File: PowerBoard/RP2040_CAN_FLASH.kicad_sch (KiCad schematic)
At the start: 48 parts, among them J1 B3B-XH-A_LF__SN_, J2 USB4145-03-0170-C_REVA2, J4 B3B-XH-A_LF__SN_, J5 Conn_02x10_Counter_Clockwise, Q1 BSS138, Q4 BSS138, U1 RPI2040, U5 W25Q128JVS, U7 MCP2515-xST, U8 MCP2551-I-SN, Y1 445C25D12M00000, Y2 CX532Z-A2B3C5-70-8.0D18

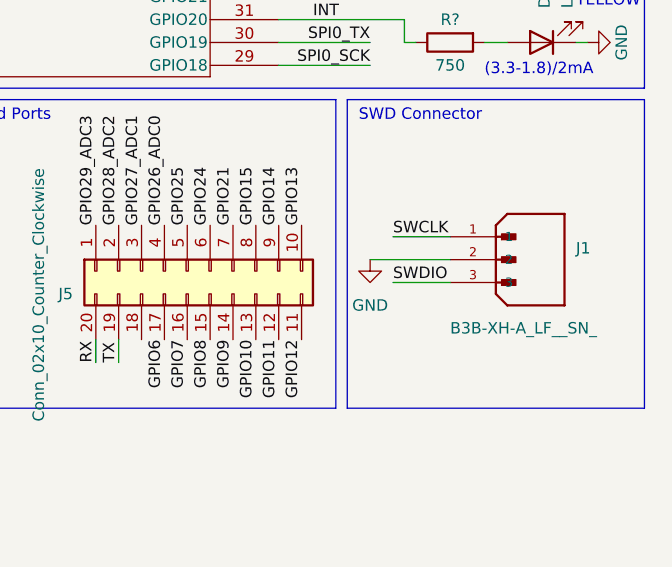
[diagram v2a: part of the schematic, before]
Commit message: layout v1 complete
- consider adding a auto discharge circuit
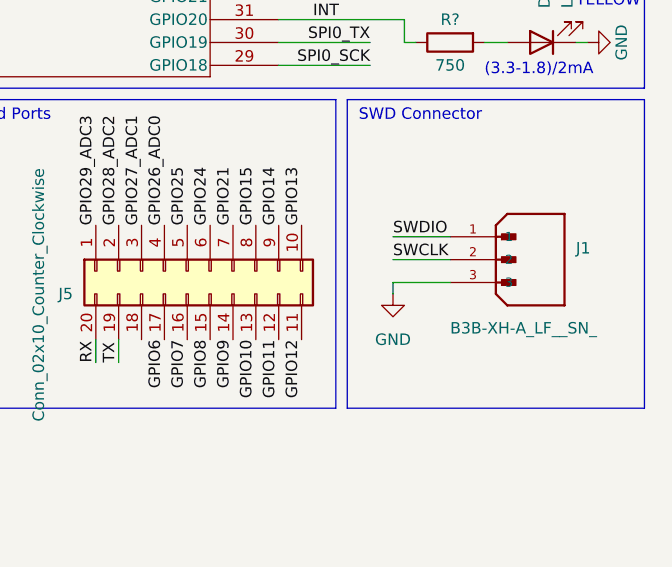
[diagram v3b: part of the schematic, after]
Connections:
- net GND: now also J1.3; no longer J1.2
- net SWCLK: now also J1.2; no longer J1.1
- net SWDIO: now also J1.1; no longer J1.3
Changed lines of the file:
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@@
+    (stroke (width 0) (type default))
+  )
+  (wire (pts (xy 251.46 149.86) (xy 257.81 149.86))
     (stroke (width 0) (type default))
   )
@@
     (stroke (width 0) (type default))
   )
-  (wire (pts (xy 248.92 147.32) (xy 257.81 147.32))
-    (stroke (width 0) (type default))
-  )
   (wire (pts (xy 88.9 175.26) (xy 82.55 175.26))
     (stroke (width 0) (type default))
@@
     (stroke (width 0) (type default))
   )
-  (wire (pts (xy 251.46 149.86) (xy 257.81 149.86))
+  (wire (pts (xy 251.46 147.32) (xy 257.81 147.32))
     (stroke (width 0) (type default))
   )
@@
   )
   (wire (pts (xy 238.76 74.93) (xy 247.65 74.93))
+    (stroke (width 0) (type default))
+  )
+  (wire (pts (xy 251.46 149.86) (xy 251.46 151.13))
     (stroke (width 0) (type default))
   )
@@
     (effects (font (size 1.27 1.27)) (justify left bottom))
   )
+  (label "SWDIO" (at 251.46 144.78 0) (fields_autoplaced)
+    (effects (font (size 1.27 1.27)) (justify left bottom))
+  )
   (label "QSPI_SCLK" (at 49.53 102.87 0) (fields_autoplaced)
     (effects (font (size 1.27 1.27)) (justify left bottom))
@@
     (effects (font (size 1.27 1.27)) (justify right bottom))
   )
-  (label "SWCLK" (at 251.46 144.78 0) (fields_autoplaced)
-    (effects (font (size 1.27 1.27)) (justify left bottom))
-  )
   (label "GPIO29_ADC3" (at 242.57 95.25 0) (fields_autoplaced)
     (effects (font (size 1.27 1.27)) (justify left bottom))
@@
     (effects (font (size 1.27 1.27)) (justify right bottom))
   )
+  (label "SWCLK" (at 251.46 147.32 0) (fields_autoplaced)
+    (effects (font (size 1.27 1.27)) (justify left bottom))
+  )
   (label "GPIO26_ADC0" (at 226.06 143.51 90) (fields_autoplaced)
-    (effects (font (size 1.27 1.27)) (justify left bottom))
-  )
-  (label "SWDIO" (at 251.46 149.86 0) (fields_autoplaced)
     (effects (font (size 1.27 1.27)) (justify left bottom))
   )
@@
     )
   )
-  (symbol (lib_id "power:GND") (at 248.92 147.32 0) (unit 1)
+  (symbol (lib_id "power:GND") (at 251.46 151.13 0) (unit 1)
     (in_bom yes) (on_board yes) (dnp no) (fields_autoplaced)
-    (property "Reference" "#PWR?" (at 248.92 153.67 0)
-      (effects (font (size 1.27 1.27)) hide)
-    )
-    (property "Value" "GND" (at 248.92 152.4 0)
-      (effects (font (size 1.27 1.27)))
-    )
-    (property "Footprint" "" (at 248.92 147.32 0)
-      (effects (font (size 1.27 1.27)) hide)
-    )
-    (property "Datasheet" "" (at 248.92 147.32 0)
-      (effects (font (size 1.27 1.27)) hide)
-    )
+    (property "Reference" "#PWR?" (at 251.46 157.48 0)
+      (effects (font (size 1.27 1.27)) hide)
+    )
+    (property "Value" "GND" (at 251.46 156.21 0)
+      (effects (font (size 1.27 1.27)))
+    )
+    (property "Footprint" "" (at 251.46 151.13 0)
+      (effects (font (size 1.27 1.27)) hide)
+    )
+    (property "Datasheet" "" (at 251.46 151.13 0)
+      (effects (font (size 1.27 1.27)) hide)
+    )

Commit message: auto discharge circuit
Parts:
- removed J4: B3B-XH-A_LF__SN_, bots:JST_B3B-XH-A_LF__SN_, symbol bots:B3B-XH-A_LF__SN_
- added TP1: SCK, bots:TestPoint_Pad_1.0x1.0mm, symbol Connector:TestPoint
- added TP1: CS, bots:TestPoint_Pad_1.0x1.0mm, symbol Connector:TestPoint
- added TP1: SO, bots:TestPoint_Pad_1.0x1.0mm, symbol Connector:TestPoint
- added TP1: RESET, bots:TestPoint_Pad_1.0x1.0mm, symbol Connector:TestPoint
- added TP1: CANL, bots:TestPoint_THTPad_D1.0mm_Drill0.5mm, symbol Connector:TestPoint
- added TP1: RXCAN, bots:TestPoint_Pad_1.0x1.0mm, symbol Connector:TestPoint
- added TP1: TXCAN, bots:TestPoint_Pad_1.0x1.0mm, symbol Connector:TestPoint
- added TP1: BOOT, bots:TestPoint_Pad_1.0x1.0mm, symbol Connector:TestPoint
- added TP1: 5V, bots:TestPoint_Pad_1.0x1.0mm, symbol Connector:TestPoint
- added TP1: SI, bots:TestPoint_Pad_1.0x1.0mm, symbol Connector:TestPoint
- added TP1: CANH, bots:TestPoint_THTPad_D1.0mm_Drill0.5mm, symbol Connector:TestPoint
- added U10, U9: PTS647SM38SMTR2LFS, SW_PTS647SM38SMTR2LFS_CNK, symbol bots:PTS647SM38SMTR2LFS
- D5: footprint bots:D_SMB -> Diode_SMD:D_SMB
- J1: footprint bots:JST_B3B-XH-A_LF__SN_ -> B3B-XH-A_LF__SN_:JST_B3B-XH-A_LF__SN_
- Q1, Q4: footprint bots:SOT95P240X111-3N -> BSS138:SOT95P240X111-3N
- U7: footprint bots:TSSOP-20_4.4x6.5mm_P0.65mm -> Package_SO:TSSOP-20_4.4x6.5mm_P0.65mm
- U8: footprint bots:SOIC-8_3.9x4.9mm_P1.27mm -> Package_SO:SOIC-8_3.9x4.9mm_P1.27mm
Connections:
- net 5V_USB: now also TP1.1
- net CANH: now also TP1.1
- net CANL: now also TP1.1
- net GND: now also U10.3, U10.4, U9.3, U9.4
- net RUN: now also TP1.1, U9.1, U9.2
- net RXCAN: now also TP1.1
- net SPI0_CS: now also TP1.1
- net SPI0_RX: now also TP1.1
- net SPI0_SCK: now also TP1.1
- net SPI0_TX: now also TP1.1
- net TXCAN: now also TP1.1
- net USB_BOOT renamed BOOT
- net BOOT: now also TP1.1, U10.1, U10.2
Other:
- note added: "BOOT BUTTON"
- note added: "RESET BUTTON"
- moved on the sheet: C?, R?, Y2

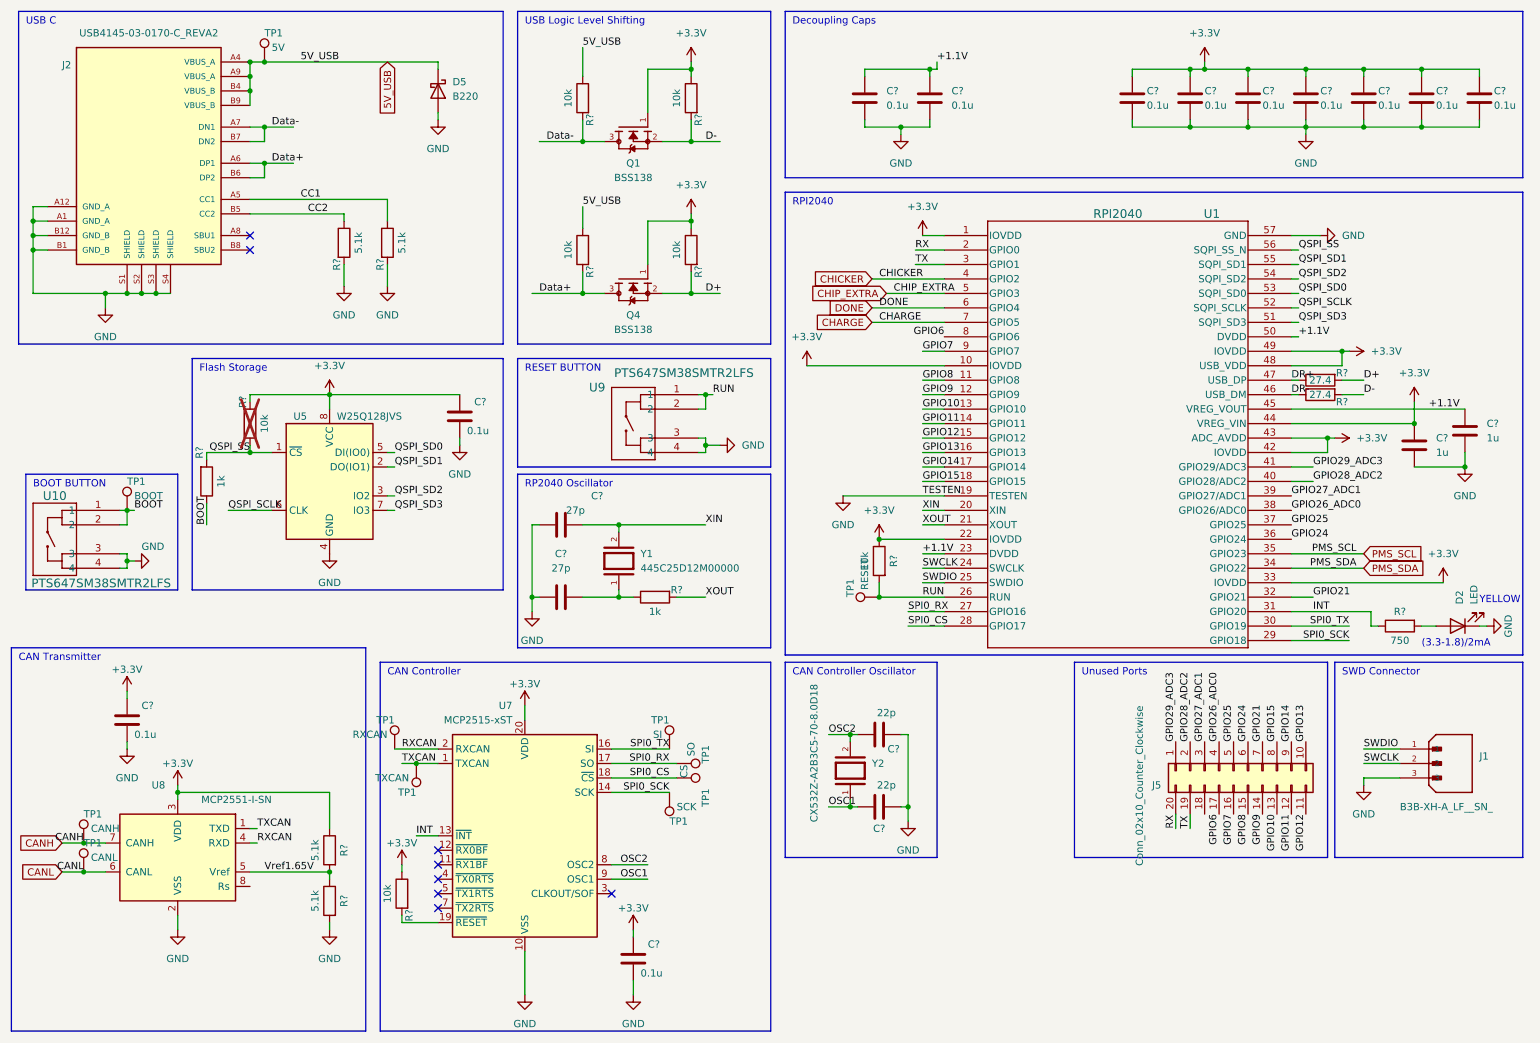
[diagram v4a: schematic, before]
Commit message: updated board edge clearance and cap model
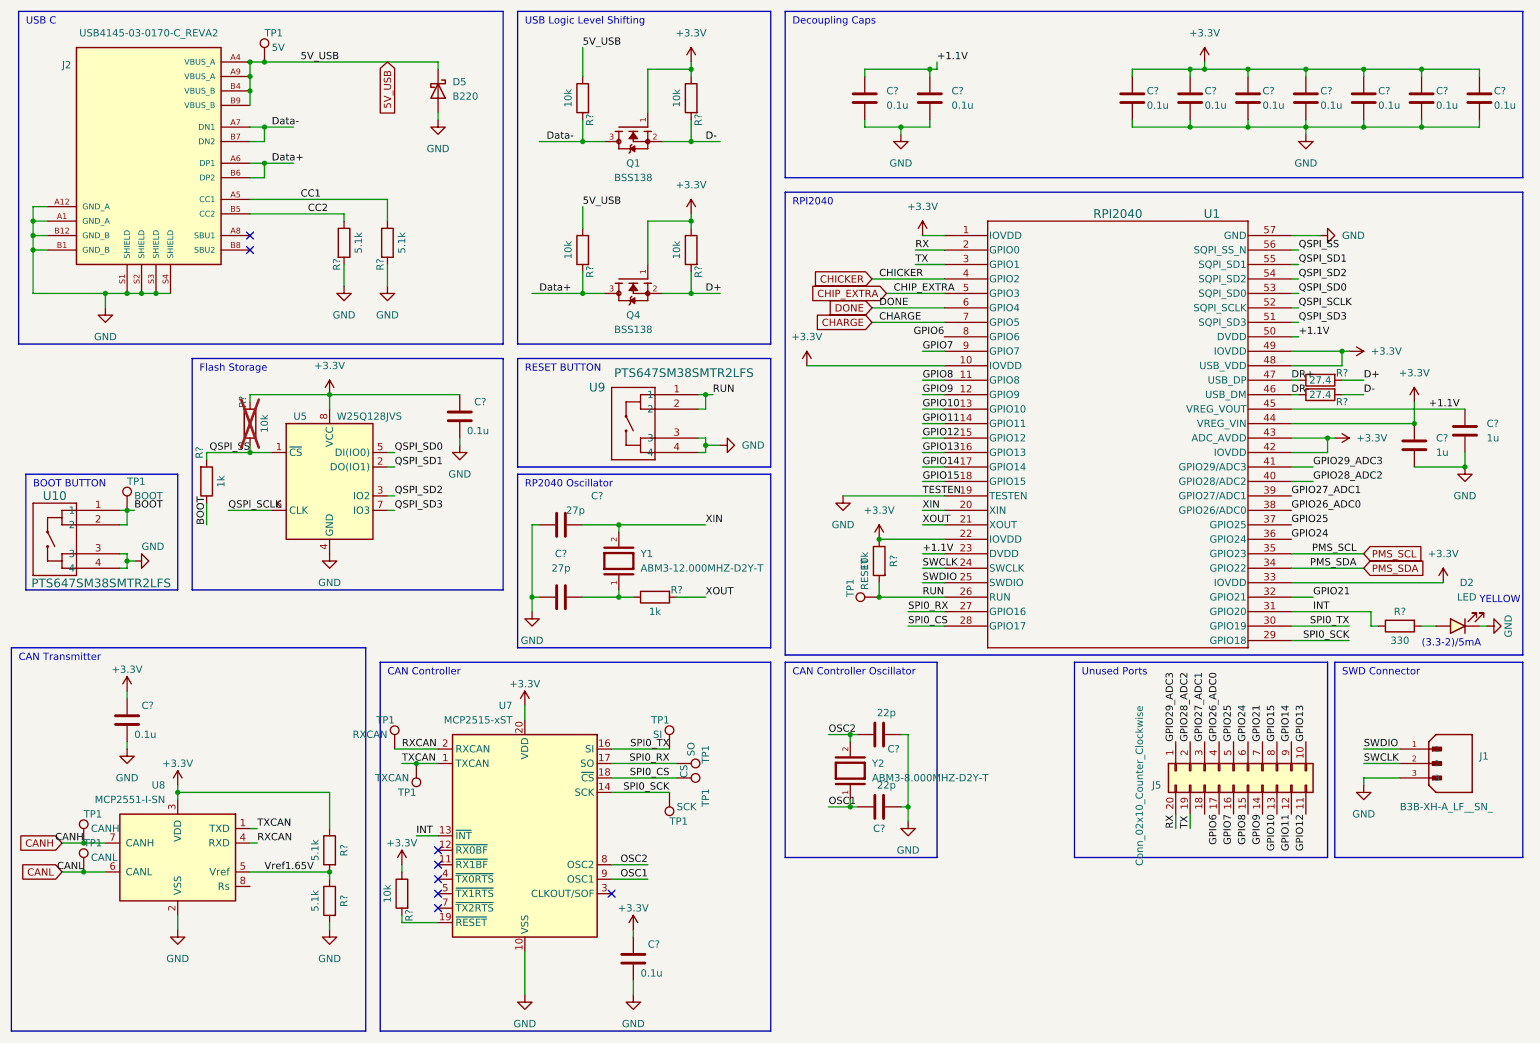
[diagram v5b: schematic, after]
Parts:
- removed D5: B220, Diode_SMD:D_SMB, symbol Diode:B220
- removed U8: MCP2551-I-SN, Package_SO:SOIC-8_3.9x4.9mm_P1.27mm, symbol Interface_CAN_LIN:MCP2551-I-SN
- removed Y1: 445C25D12M00000, bots:445C25D12M00000, symbol bots:445C25D12M00000
- removed Y2: CX532Z-A2B3C5-70-8.0D18, bots:445C25D12M00000, symbol bots:CX532Z-A2B3C5-70-8.0D18
- added D5: B220, bots:D_SMB, symbol bots:B220
- added U8: MCP2551-I-SN, bots:SOIC-8_3.9x4.9mm_P1.27mm, symbol bots:MCP2551-I-SN
- added Y1: ABM3-12.000MHZ-D2Y-T, bots:ABM3, symbol bots:ABM3-12.000MHZ-D2Y-T
- added Y2: ABM3-8.000MHZ-D2Y-T, bots:445C25D12M00000, symbol bots:ABM3-8.000MHZ-D2Y-T
- C? (x2): symbol Device:C -> bots:C_22p; JLC (none) -> 0603; LCSC (none) -> C1653; MPN (none) -> CL10C220JB8NNNC; Manufacturer (none) -> Samsung Electro-Mechanics; Price (none) -> 0.0052
- C? (x12): symbol Device:C -> bots:C_0.1u; JLC (none) -> 0603; LCSC (none) -> C14663; MPN (none) -> CC0603KRX7R9BB104; Manufacturer (none) -> YAGEO; Price (none) -> 0.0021
- C? (x2): symbol Device:C -> bots:C_1u; JLC (none) -> 0603; LCSC (none) -> C15849; MPN (none) -> CL10A105KB8NNNC; Manufacturer (none) -> Samsung Electro-Mechanics; Price (none) -> 0.0046
- C? (x2): symbol Device:C -> bots:C_27p; JLC (none) -> 0603; LCSC (none) -> C107045; MPN (none) -> CC0603JRNPO9BN270; Manufacturer (none) -> YAGEO; Price (none) -> 0.0027
- D2: footprint bots:LED_1206_3216Metric -> bots:LED_0603_1608Metric; symbol Device:LED -> bots:LED_yellow; JLC (none) -> 0603; LCSC (none) -> C409441; MPN (none) -> 19-21UYC/S530-A4/TR8; Manufacturer (none) -> Everlight Elec; Price (none) -> 0.0404
- J1: footprint B3B-XH-A_LF__SN_:JST_B3B-XH-A_LF__SN_ -> bots:JST_B3B-XH-A_LF__SN_; Availability In Stock -> (none); Check_prices https://www.snapeda.com/parts/B3B-XH-A(LF)(SN)/JST+Sales+Am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 -> (none); MANUFACTURER JST Sales America Inc. -> (none); MAXIMUM_PACKAGE_HEIGHT 7 mm -> (none); MF JST Sales -> (none); MP B3B-XH-A(LF)(SN) -> (none); MPN (none) -> B3B-XH-A(LF)(SN); Manufacturer (none) -> JST Sales America Inc.; PARTREV N/A -> (none); Package None -> (none); Price None -> 0.31; SNAPEDA_PN B3B-XH-A(LF)(SN) -> (none); STANDARD Manufacturer Recommendations -> (none); SnapEDA_Link https://www.snapeda.com/parts/B3B-XH-A(LF)(SN)/JST+Sales+Am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 -> (none)
- J2: Availability In Stock -> (none); Check_prices https://www.snapeda.com/parts/USB4145-03-0170-C/Global+Conn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 -> (none); MANUFACTURER GCT -> (none); MAXIMUM_PACKAGE_HEIGHT 7.66mm -> (none); MF Global Connector Technology -> (none); MP USB4145-03-0170-C -> (none); MPN (none) -> USB4145-03-0170-C; Manufacturer (none) -> GCT; PARTREV A2 -> (none); Package None -> (none); Price None -> 1.61; SNAPEDA_PN USB4145-03-0170-C -> (none); STANDARD Manufacturer Recommendations -> (none); SnapEDA_Link https://www.snapeda.com/parts/USB4145-03-0170-C/Global+Conn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 -> (none)
- Q1, Q4: footprint BSS138:SOT95P240X111-3N -> bots:SOT95P240X111-3N; AVAILABILITY In Stock -> (none); Availability In Stock -> (none); Check_prices https://www.snapeda.com/parts/BSS138/Diodes+Inc./view-part/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 -> (none); DESCRIPTION N-Channel 50 V 200mA (Ta) 225mW (Ta) Surface Mount SOT-23-3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 -> (none); JLC (none) -> SOT-23; LCSC (none) -> C52895; MF Diodes Inc. -> (none); MP BSS138 -> (none); MPN (none) -> BSS138; Manufacturer (none) -> onsemi; PACKAGE SOT-23 ON -> (none); PRICE None -> (none); Package SOT-23-3 Diodes Inc. -> SOT-23; Price None -> 0.51; SnapEDA_Link https://www.snapeda.com/parts/BSS138/Diodes+Inc./view-part/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 -> (none)
- R?: value 750 -> 330; symbol Device:R -> bots:R_330R; JLC (none) -> 0603; LCSC (none) -> C23138; MPN (none) -> 0603WAF3300T5E; Manufacturer (none) -> UNI-ROYAL(Uniroyal Elec); Price (none) -> 0.0009
- R? (x4): symbol Device:R -> bots:R_5.1k; JLC (none) -> 0603; LCSC (none) -> C23186; MPN (none) -> 0603WAF5101T5E; Manufacturer (none) -> UNI-ROYAL(Uniroyal Elec); Price (none) -> 0.0009
- R? (x2): symbol Device:R -> bots:R_27.4R; JLC (none) -> 0603; LCSC (none) -> C22926; MPN (none) -> 0603WAF274JT5E; Manufacturer (none) -> UNI-ROYAL(Uniroyal Elec); Price (none) -> 0.001
- R? (x6): symbol Device:R -> bots:R_10k; JLC (none) -> 0603; LCSC (none) -> C25804; MPN (none) -> 0603WAF1002T5E; Manufacturer (none) -> UNI-ROYAL(Uniroyal Elec); Price (none) -> 0.0008
- R? (x2): symbol Device:R -> bots:R_1k; JLC (none) -> 0603; LCSC (none) -> C21190; MPN (none) -> 0603WAF1001T5E; Manufacturer (none) -> UNI-ROYAL(Uniroyal Elec); Price (none) -> 0.0007
- R?: footprint Resistor_SMD:R_0603_1608Metric -> bots:R_0603_1608Metric; symbol Device:R -> bots:R_10k; JLC (none) -> 0603; LCSC (none) -> C25804; MPN (none) -> 0603WAF1002T5E; Manufacturer (none) -> UNI-ROYAL(Uniroyal Elec); Price (none) -> 0.0008
- TP1: symbol Connector:TestPoint -> bots:TestPoint_1x1; now left out of the parts list
- TP1: symbol Connector:TestPoint -> bots:TestPoint_1x1drill; now left out of the parts list
- U1: JLC (none) -> LQFN-56(7x7); LCSC (none) -> C2040; MPN (none) -> RP2040; Manufacturer (none) -> Raspberry Pi; Price (none) -> 0.9997
- U10, U9: footprint SW_PTS647SM38SMTR2LFS_CNK -> bots:SW_PTS647SM38SMTR2LFS_CNK; JLC (none) -> SMD,4.5x4.5mm; LCSC (none) -> C2689502; MPN (none) -> PTS647SM38SMTR2LFS; Manufacturer (none) -> C&K; Price (none) -> 0.1118
- U5: symbol bots:W25Q128JVS -> bots:W25Q16JVSNIQ; JLC (none) -> SOIC-8-208mil; LCSC (none) -> C97521; MPN (none) -> W25Q128JVSIQ; Manufacturer (none) -> Winbond Elec; Price (none) -> 0.5635
- U7: footprint Package_SO:TSSOP-20_4.4x6.5mm_P0.65mm -> bots:TSSOP-20_4.4x6.5mm_P0.65mm; symbol Interface_CAN_LIN:MCP2515-xST -> bots:MCP2515T-I/ST; JLC (none) -> TSSOP-20; LCSC (none) -> C185941; MPN (none) -> MCP2515T-I/ST; Manufacturer (none) -> Microchip; Price (none) -> 1.2541
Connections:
- net +3.3V: now also U8.3 (VDD)
- net 5V_USB: now also D5.1 (K)
- net CANH: now also U8.7 (CANH)
- net CANL: now also U8.6 (CANL)
- net GND: now also D5.2 (A), U8.2 (VSS)
- net OSC1: now also Y2.1
- net OSC2: now also Y2.2
- net RXCAN: now also U8.4 (RXD)
- net TXCAN: now also U8.1 (TXD)
- net Vref1.65V: now also U8.5 (Vref)
- net XIN: now also Y1.2
- net at C?.2, R?.1: now also Y1.1
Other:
- note added: "(3.3-2)/5mA"
- note removed: "(3.3-1.8)/2mA"
